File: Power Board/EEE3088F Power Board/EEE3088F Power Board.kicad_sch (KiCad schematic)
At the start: 28 parts, among them J1 Conn_02x16_Odd_Even, Q1 2N7002, U1 INA219AxDCN, U2 LM2596S-5, U3 TP4056-42-ESOP8, U4 DRV8837, U5 DRV8837, U6 DRV8837, U7 DRV8837

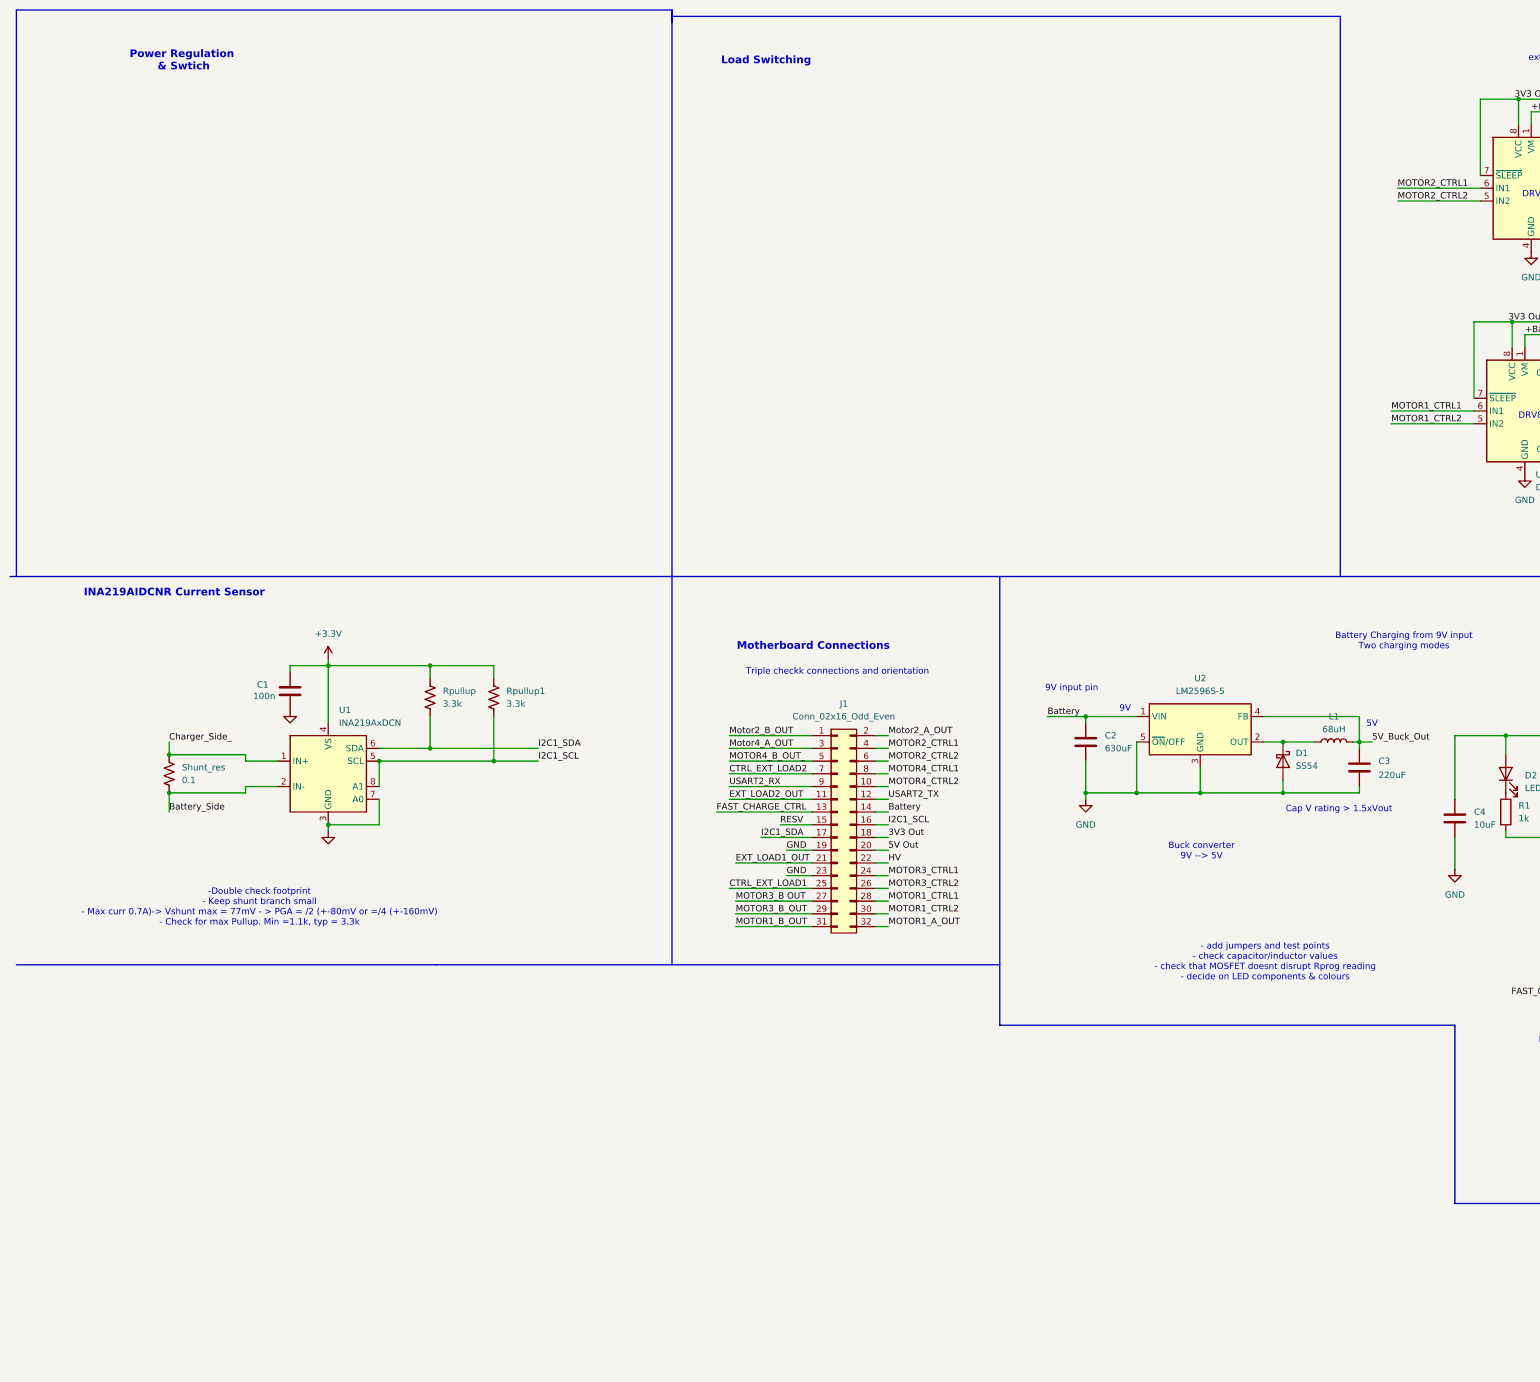
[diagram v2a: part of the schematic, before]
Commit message: 3v3 and some footprints complete
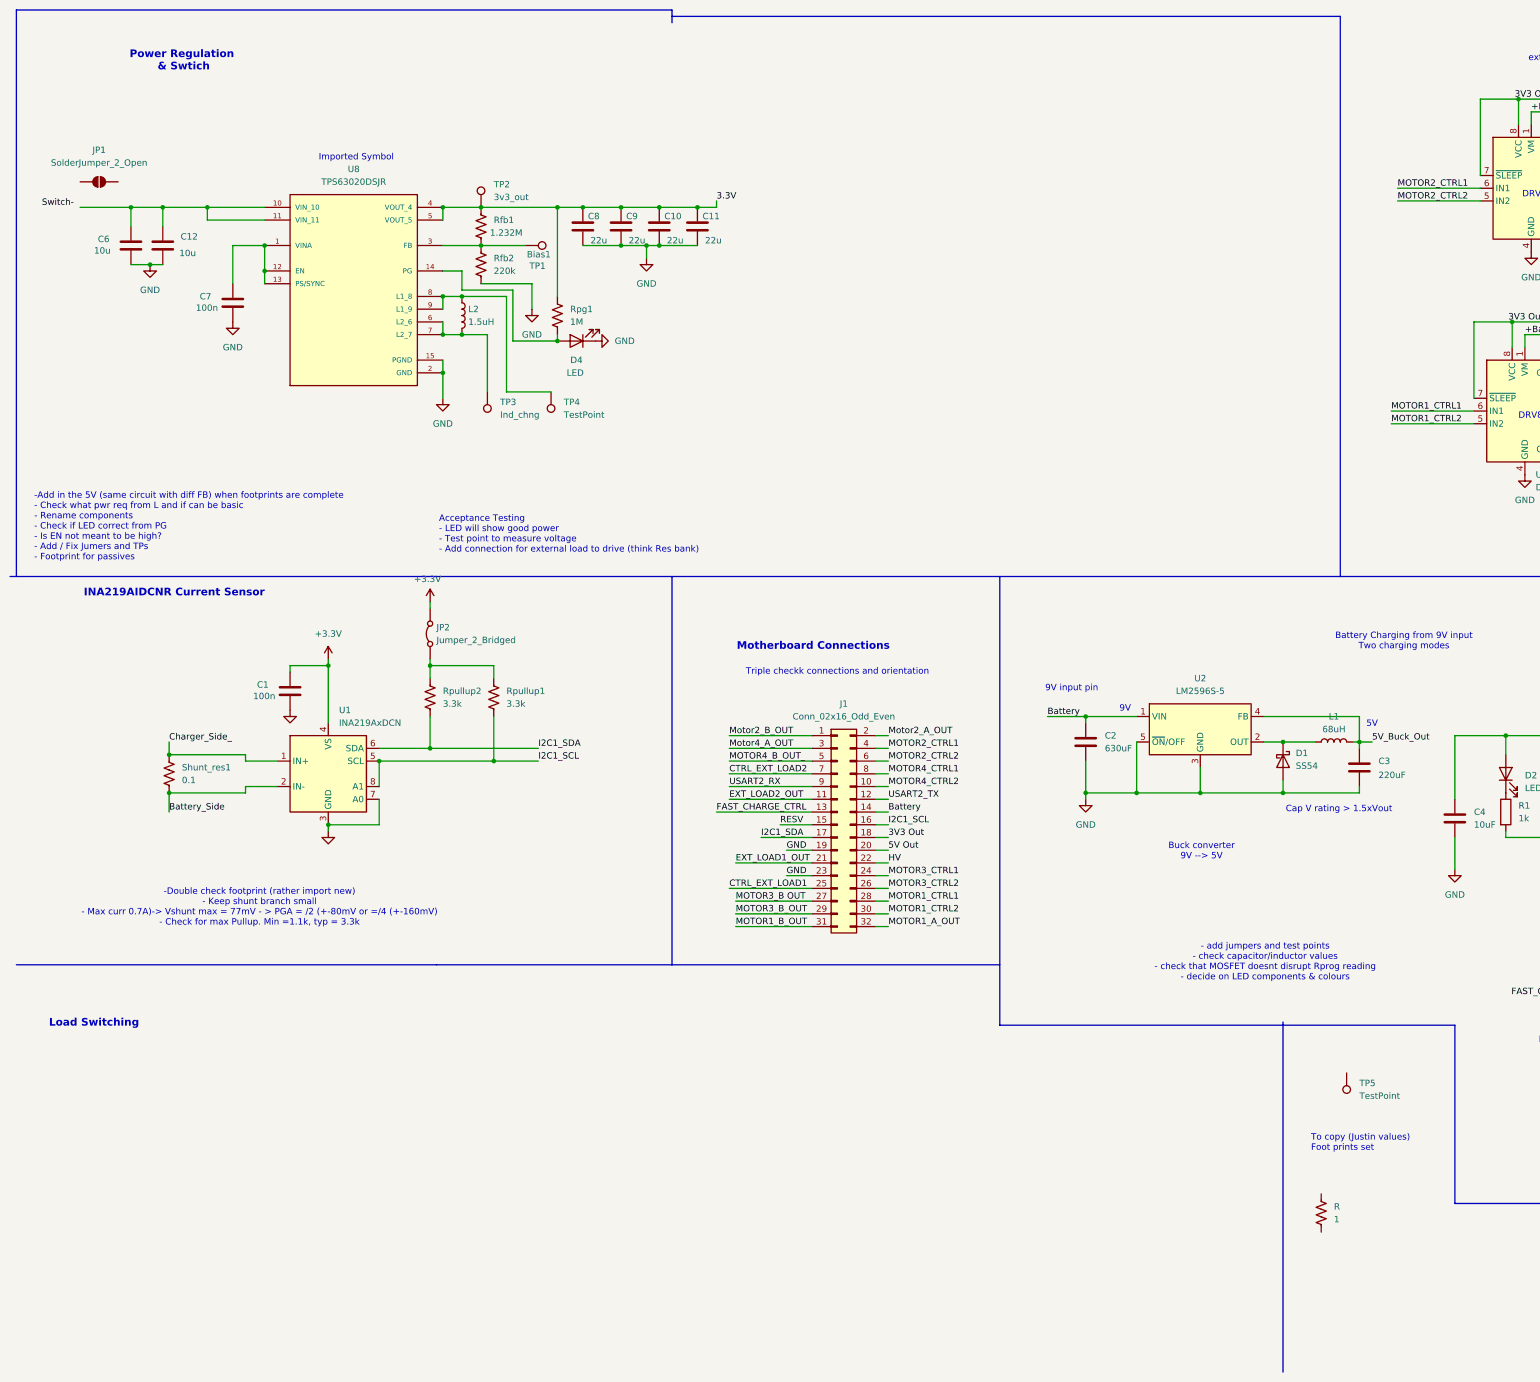
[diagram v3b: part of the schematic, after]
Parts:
- added C10, C11, C8, C9: 22u, symbol Device:C
- added C12, C6: 10u, symbol Device:C
- added C7: 100n, symbol Device:C
- added D4: LED, symbol Device:LED
- added JP1: SolderJumper_2_Open, symbol Jumper:SolderJumper_2_Open
- added JP2: Jumper_2_Bridged, TestPoint:TestPoint_Pad_D2.0mm, symbol Jumper:Jumper_2_Bridged
- added L2: 1.5uH, symbol Device:L
- added R: 1, Resistor_SMD:R_0402_1005Metric_Pad0.72x0.64mm_HandSolder, symbol Device:R_US
- added Rfb1: 1.232M, symbol Device:R_US
- added Rfb2: 220k, symbol Device:R_US
- added Rpg1: 1M, symbol Device:R_US
- added TP1: Bias1, symbol Connector:TestPoint
- added TP2: 3v3_out, symbol Connector:TestPoint
- added TP3: Ind_chng, symbol Connector:TestPoint
- added TP4: TestPoint, symbol Connector:TestPoint
- added TP5: TestPoint, TestPoint:TestPoint_Pad_D2.0mm, symbol Connector:TestPoint
- added U8: TPS63020DSJR, TPS63020DSJR:IC_TPS63020DSJR, symbol TPS63020DSJR:TPS63020DSJR
- renumbered Rpullup to Rpullup2, Shunt_res to Shunt_res1
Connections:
- net +3.3V: now also JP2.2 (B); no longer Rpullup1.1, Rpullup2.1
- net GND: now also C10.1, C11.1, C12.1, C6.1, C7.1, C8.1, C9.1, D4.1 (K), Rfb2.2, U8.15 (PGND), U8.2 (GND)
- new net: D4.2 (A), Rpg1.2, U8.14 (PG)
- new net: JP2.1 (A), Rpullup1.1, Rpullup2.1
- new net: L2.2, TP3.1, U8.6 (L2_6), U8.7 (L2_7)
- new net: L2.1, TP4.1, U8.8 (L1_8), U8.9 (L1_9)
- new net: Rfb1.2, Rfb2.1, TP1.1, U8.3 (FB)
- new net: C7.2, U8.1 (VINA), U8.12 (EN), U8.13 (PS/SYNC)
- new net: C12.2, C6.2, U8.10 (VIN_10), U8.11 (VIN_11)
- new net 3.3V: C10.2, C11.2, C8.2, C9.2, Rfb1.1, Rpg1.1, TP2.1, U8.4 (VOUT_4), U8.5 (VOUT_5)
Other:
- note added: "-Add in the 5V (same circuit with diff FB) when footprints are complete - Check what pwr req from L and if can be basic - Rename components - Check if LED correct from PG - Is EN not meant to be high? - Add / Fix Jumers and TPs - Footprint for passives"
- note added: "-Double check footprint (rather import new) - Keep shunt branch small - Max curr 0.7A)-> Vshunt max = 77mV - > PGA = /2 (+-80mV or =/4 (+-160mV) - Check for max Pullup. Min =1.1k, typ = 3.3k"
- note added: "Acceptance Testing - LED will show good power - Test point to measure voltage - Add connection for external load to drive (think Res bank)"
- note added: "Imported Symbol"
- note added: "To copy (Justin values) Foot prints set"
- note removed: "-Double check footprint - Keep shunt branch small - Max curr 0.7A)-> Vshunt max = 77mV - > PGA = /2 (+-80mV or =/4 (+-160mV) - Check for max Pullup. Min =1.1k, typ = 3.3k"

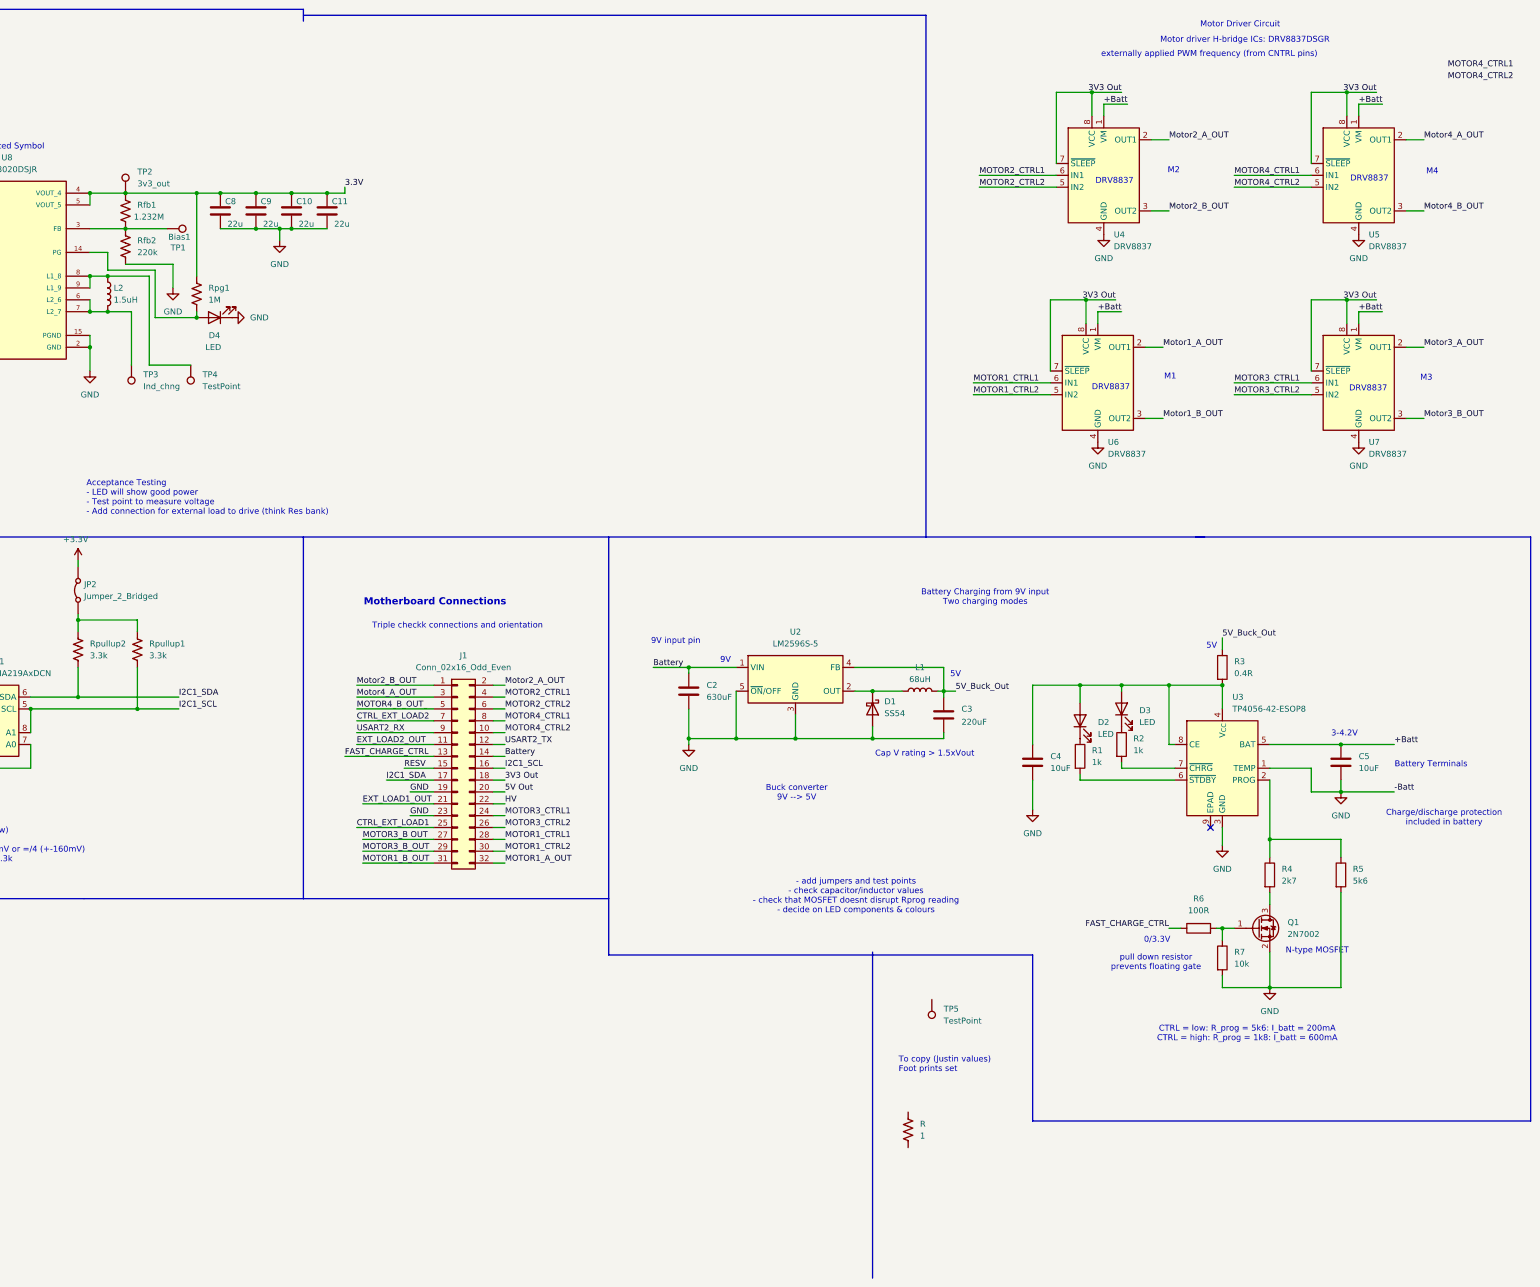
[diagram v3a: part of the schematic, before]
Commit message: Finished USB Type-C, added test points
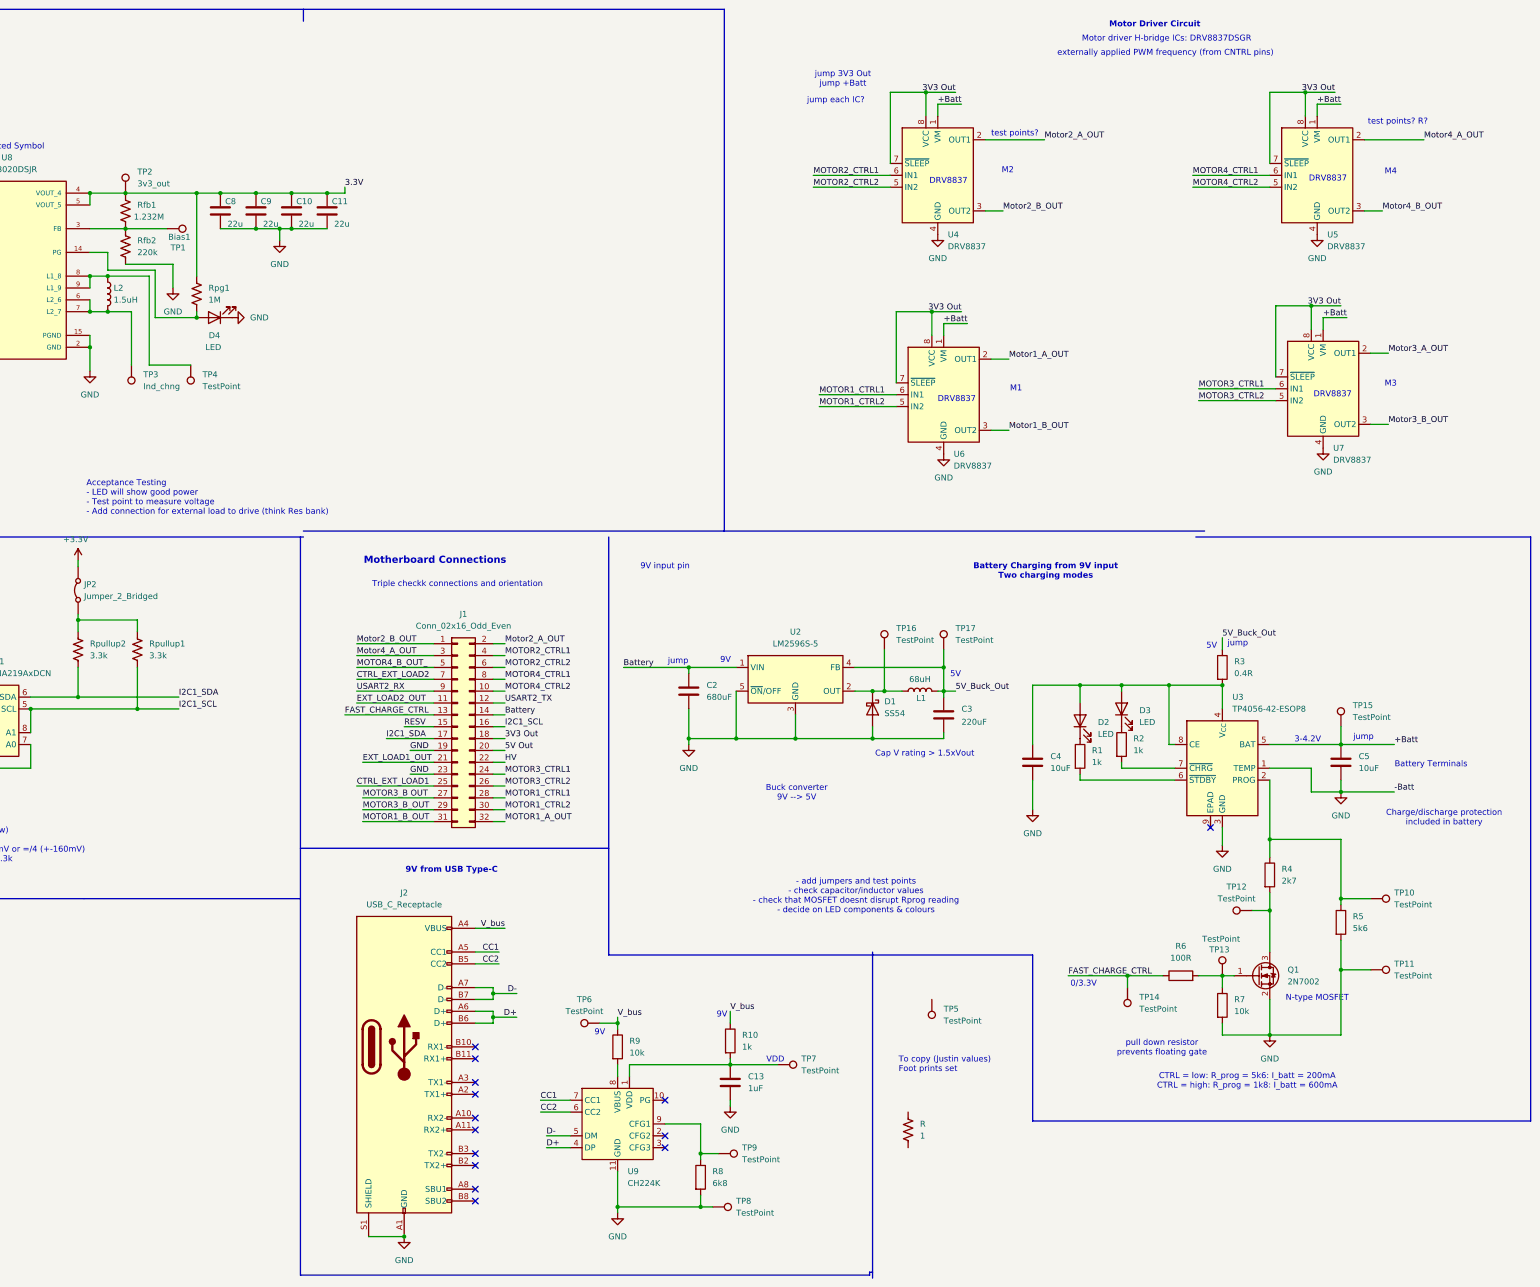
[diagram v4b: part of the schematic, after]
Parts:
- added C13: 1uF, symbol Device:C
- added J2: USB_C_Receptacle, symbol Connector:USB_C_Receptacle
- added R10: 1k, symbol Device:R
- added R8: 6k8, symbol Device:R
- added R9: 10k, symbol Device:R
- added TP10, TP11, TP12, TP13, TP14, TP15, TP16, TP17, TP6, TP7, TP8, TP9: TestPoint, TestPoint:TestPoint_Pad_D2.0mm, symbol Connector:TestPoint
- added U9: CH224K, Package_SO:SSOP-10-1EP_3.9x4.9mm_P1mm_EP2.1x3.3mm, symbol Interface_USB:CH224K
- C2: value 630uF -> 680uF
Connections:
- net +Batt: now also TP15.1
- net 5V_Buck_Out: now also TP17.1
- net FAST_CHARGE_CTRL: now also TP14.1
- net GND: now also C13.2, J2.A1 (GND), J2.A12 (GND), J2.B1 (GND), J2.B12 (GND), J2.S1 (SHIELD), R8.2, TP11.1, TP8.1, U9.11 (GND)
- net at R4.1, R5.1, U3.2 (PROG): now also TP10.1
- net at Q1.1 (G), R6.2, R7.1: now also TP13.1
- net at Q1.3 (D), R4.2: now also TP12.1
- net at D1.1 (K), L1.1, U2.2 (OUT): now also TP16.1
- new net: C13.1, R10.2, TP7.1, U9.1 (VDD)
- new net: R9.2, U9.8 (VBUS)
- new net: R8.1, TP9.1, U9.9 (CFG1)
- new net CC1: J2.A5 (CC1), U9.7 (CC1)
- new net CC2: J2.B5 (CC2), U9.6 (CC2)
- new net D+: J2.A6 (D+), J2.B6 (D+), U9.4 (DP)
- new net D-: J2.A7 (D-), J2.B7 (D-), U9.5 (DM)
- new net V_bus: J2.A4 (VBUS), J2.A9 (VBUS), J2.B4 (VBUS), J2.B9 (VBUS), R10.1, R9.1, TP6.1
- no-connect marks 1 -> 14
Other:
- note added: "9V from USB Type-C"
- note added: "VDD"
- note added: "jump"
- note added: "jump 3V3 Out jump +Batt"
- note added: "jump each IC?"
- note added: "test points?"
- note added: "test points? R?"
- moved on the sheet: J1, Q1, R5, R6, R7, U4, U5, U6, U7
